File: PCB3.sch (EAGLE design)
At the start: 138 parts, among them U1 PIC32MX570F512L, Y1 16MHz

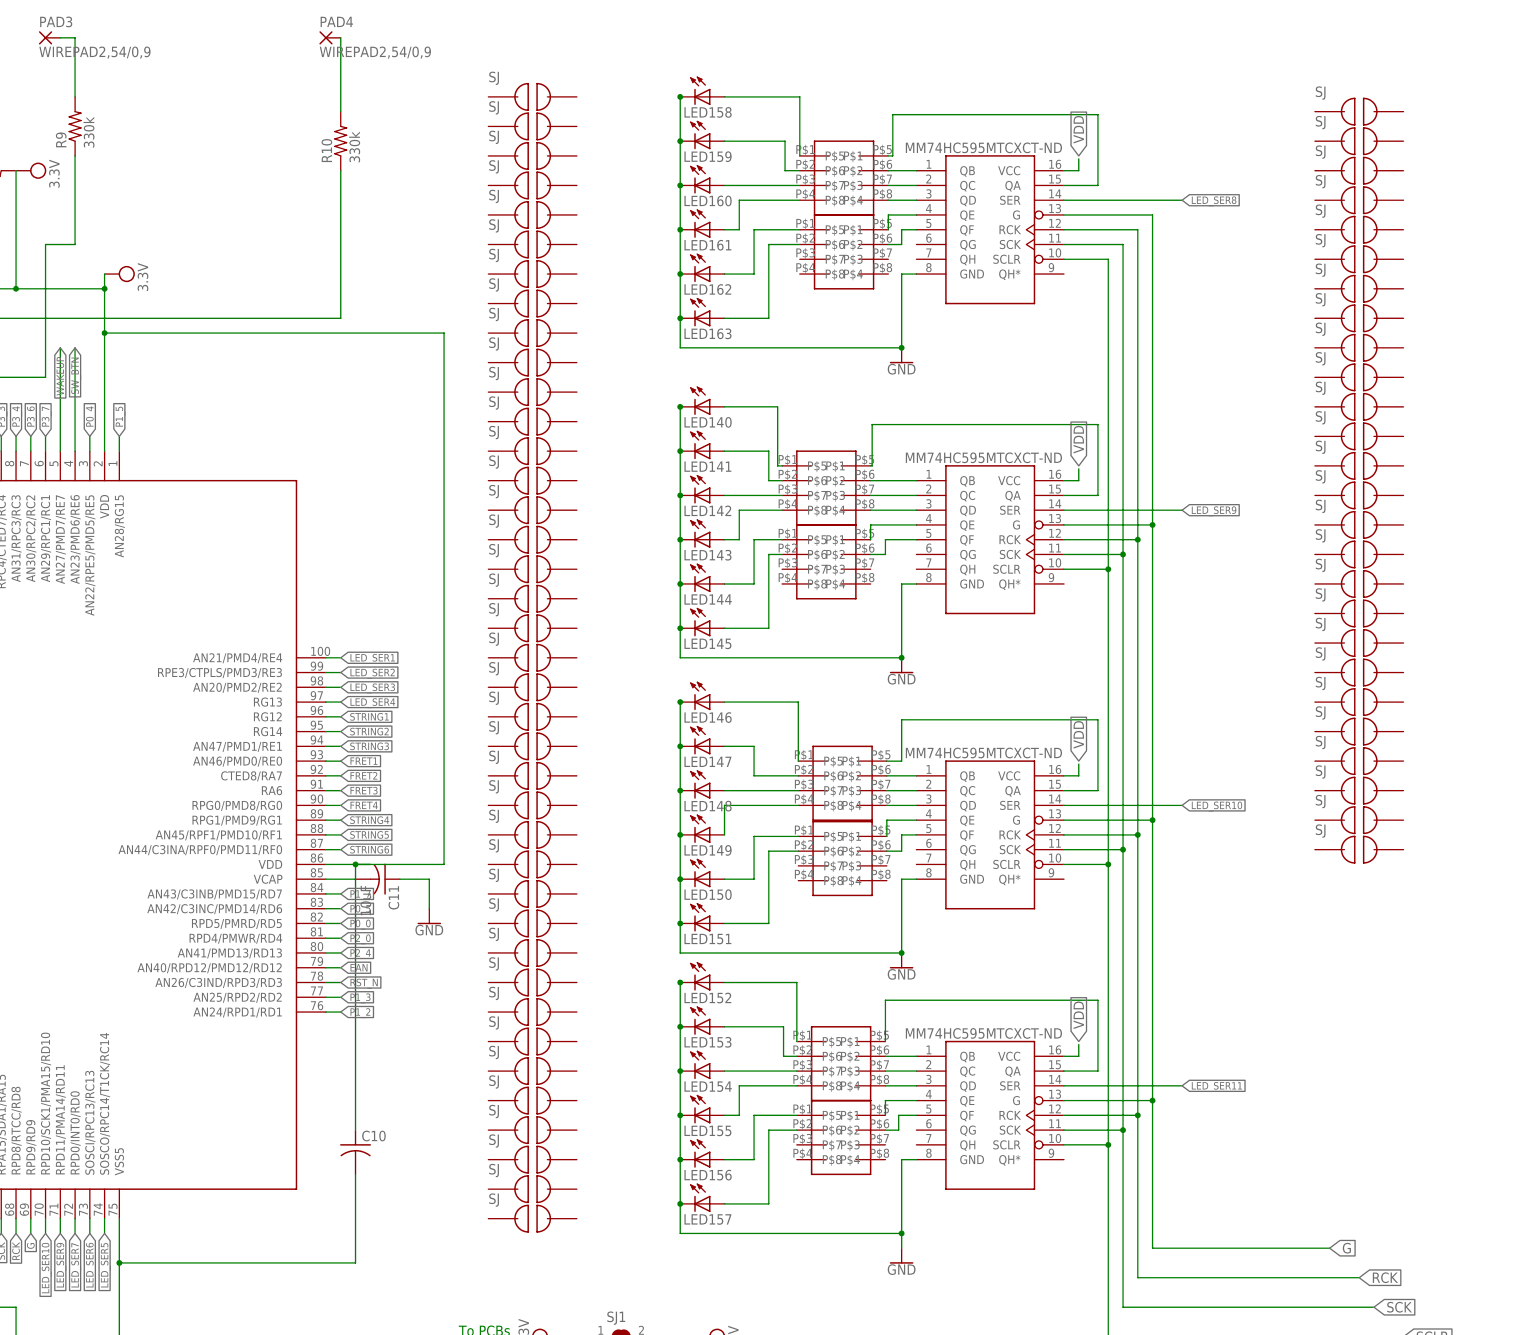
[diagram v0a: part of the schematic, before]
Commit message: Finished PCB3 checks and added traces for shift registers
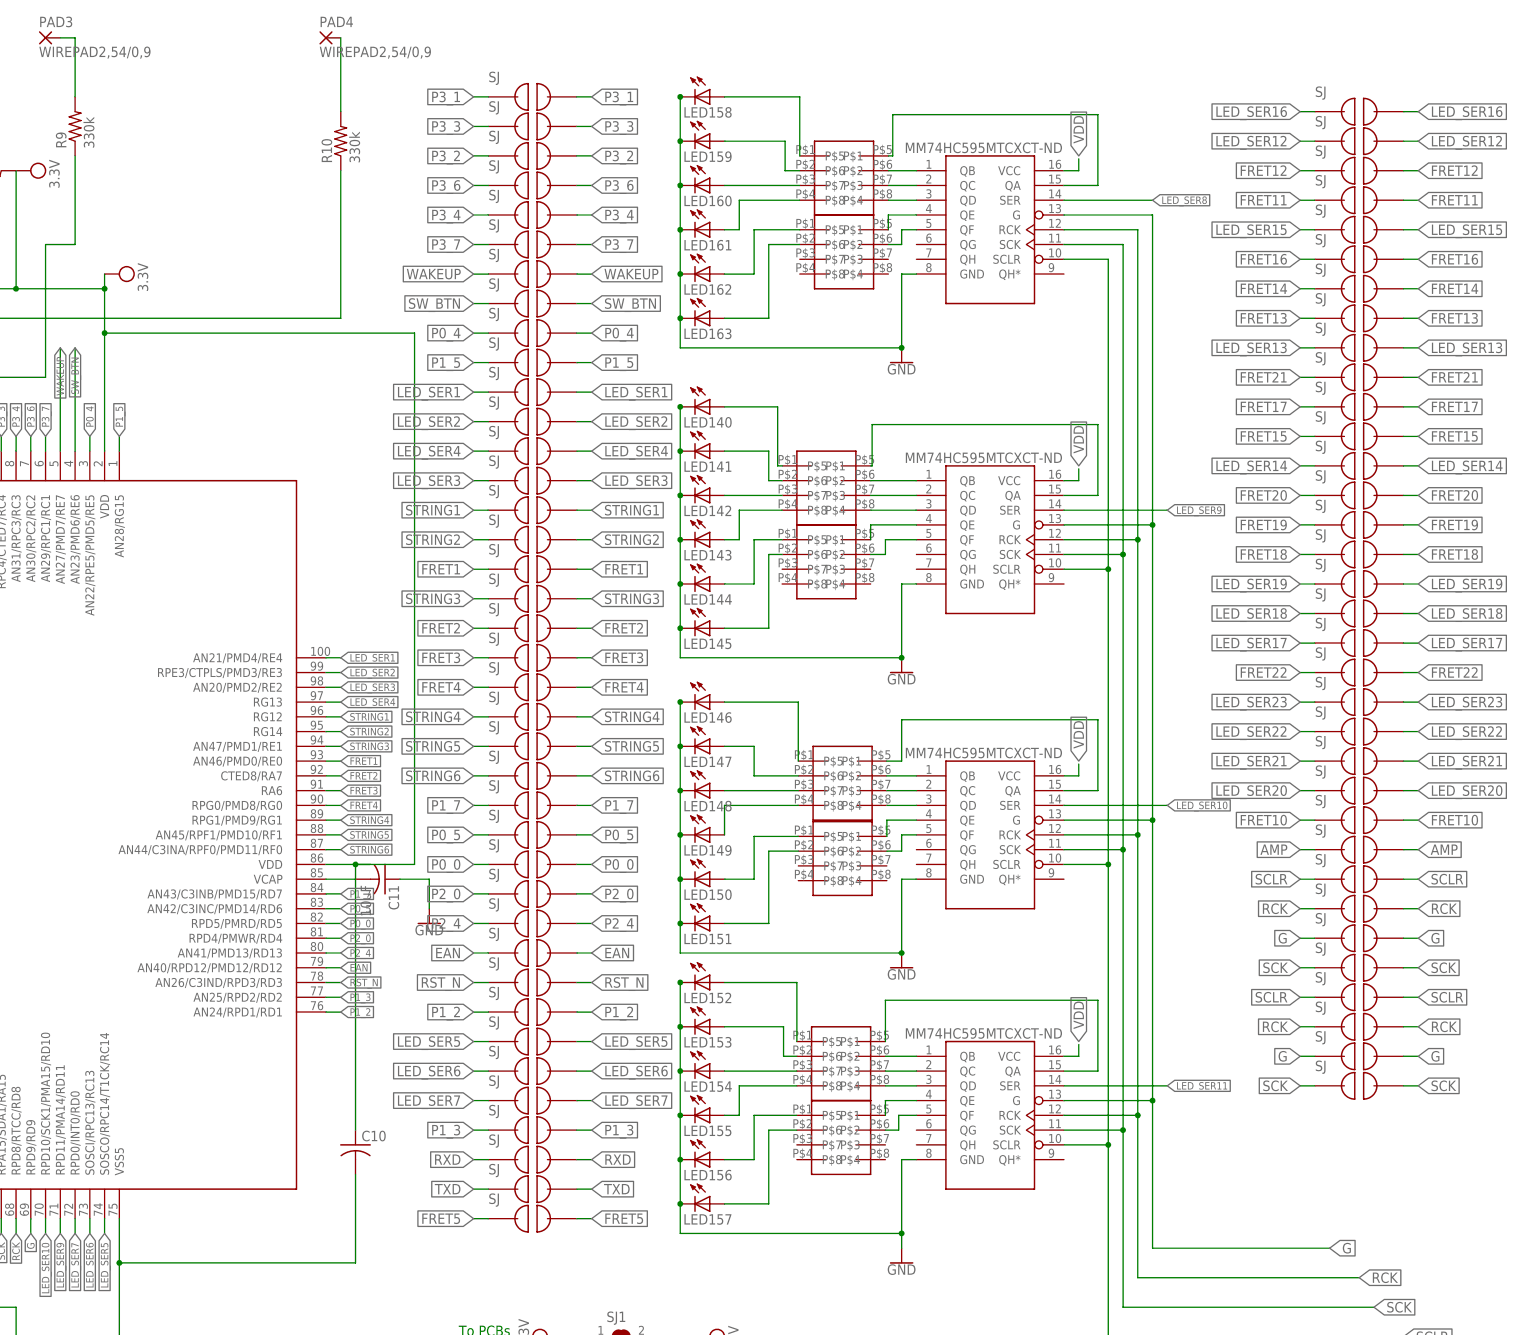
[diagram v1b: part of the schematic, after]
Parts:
- added RXD, U$2, U$79, U$80, U$81, U$82, U$83, U$84: JUMPER, ECE477_Guitutar:JUMPER
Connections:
- net AMP: now also U$70.P$2
- net EAN: now also U$35.P$2
- net FRET1: now also U$18.P$2
- net FRET10: now also U$69.P$2
- net FRET11: now also U$48.P$2
- net FRET12: now also U$47.P$2
- net FRET13: now also U$52.P$2
- net FRET14: now also U$51.P$2
- net FRET15: now also U$56.P$2
- net FRET16: now also U$50.P$2
- net FRET17: now also U$55.P$2
- net FRET18: now also U$60.P$2
- net FRET19: now also U$59.P$2
- net FRET2: now also U$20.P$2
- net FRET20: now also U$58.P$2
- net FRET21: now also U$54.P$2
- net FRET22: now also U$64.P$2
- net FRET3: now also U$21.P$2
- net FRET4: now also U$22.P$2
- net FRET5: now also U$43.P$1, U$43.P$2
- net G: now also U$80.P$2, U$84.P$2
- net LED_SER1: now also U$12.P$2
- net LED_SER12: now also U$46.P$2
- net LED_SER13: now also U$53.P$2
- net LED_SER14: now also U$57.P$2
- net LED_SER15: now also U$49.P$2
- net LED_SER16: now also U$45.P$2
- net LED_SER17: now also U$63.P$2
- net LED_SER18: now also U$62.P$2
- net LED_SER19: now also U$61.P$2
- net LED_SER2: now also U$13.P$2
- net LED_SER20: now also U$68.P$2
- net LED_SER21: now also U$67.P$2
- net LED_SER22: now also U$66.P$2
- net LED_SER23: now also U$65.P$2
- net LED_SER3: now also U$15.P$2
- net LED_SER4: now also U$14.P$2
- net LED_SER5: now also U$38.P$2
- net LED_SER6: now also U$39.P$2
- net LED_SER7: now also U$40.P$2
- net P0_0: now also U$32.P$2
- net P0_4: now also U$10.P$2
- net P0_5: now also U$31.P$2
- net P1_2: now also U$37.P$2
- net P1_3: now also U$41.P$2
- net P1_5: now also U$11.P$2
- net P1_7: now also U$30.P$2
- net P2_0: now also U$33.P$2
- net P2_4: now also U$34.P$2
- net P3_1: now also U$1.P$2
- net P3_2: now also U$4.P$2
- net P3_3: now also U$3.P$2
- net P3_4: now also U$6.P$2
- net P3_6: now also U$5.P$2
- net P3_7: now also U$7.P$2
- net RCK: now also U$79.P$2, U$83.P$2
- net RST_N: now also U$36.P$2
- net RXD: now also RXD.P$1, RXD.P$2
- net SCK: now also U$42.P$1, U$42.P$2, U$81.P$1, U$81.P$2
- net SCLR: now also U$2.P$2, U$82.P$2
- net STRING1: now also U$16.P$2
- net STRING2: now also U$17.P$2
- net STRING3: now also U$19.P$2
- net STRING4: now also U$23.P$2
- net STRING5: now also U$24.P$2
- net STRING6: now also U$25.P$2
- net SW_BTN: now also U$9.P$2
- net TXD: now also U$44.P$1, U$44.P$2
- net WAKEUP: now also U$8.P$2
